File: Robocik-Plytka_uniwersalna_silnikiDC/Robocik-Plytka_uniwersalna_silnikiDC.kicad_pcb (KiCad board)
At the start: 2 copper layers, 66 parts, among them IC1 ACSL-6400-00TE, IC2 L6205D, J1 Conn_01x08, J2 Conn_01x02, J4 Conn_01x02, J6 Conn_01x02, Q1 BC847, Q2 BC847, Q3 BC847, U1 STM32F103C8Tx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

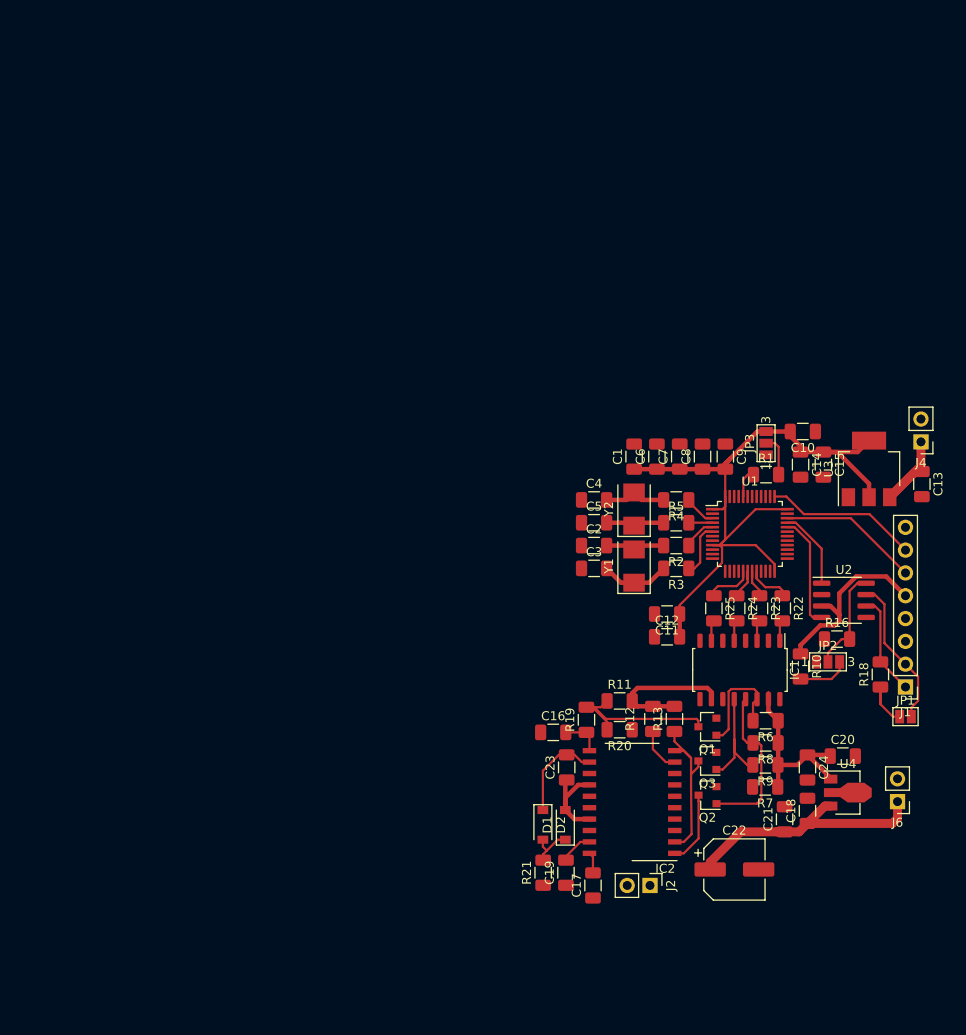
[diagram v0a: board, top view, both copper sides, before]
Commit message: Changed power supply line on schematic, added missing connections on PCB layout, added second layer connections and vias. Added layout drawing and updated schematic drawing
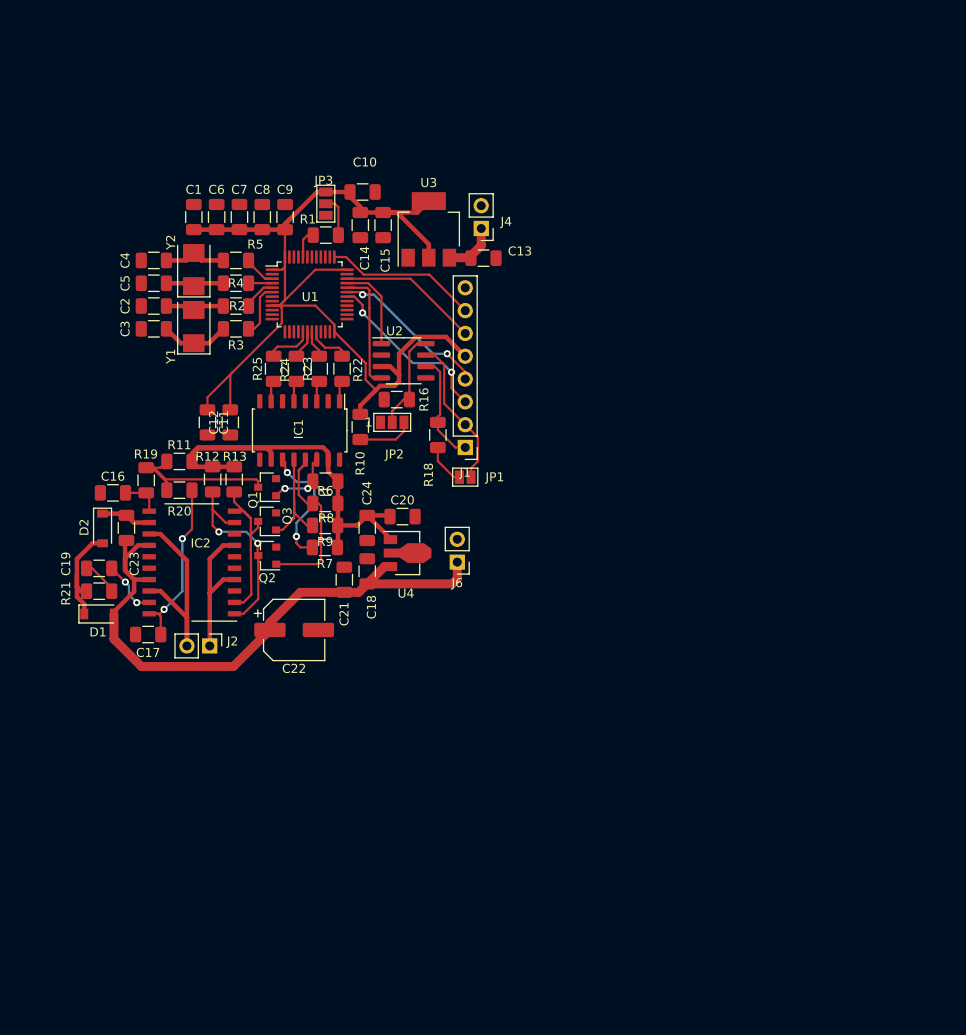
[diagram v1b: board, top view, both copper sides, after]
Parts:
- moved C19 62.1 mm to (130.9, 126.2), turned to 0 degrees
- moved D2 59.1 mm to (131.3, 121.8)
- moved R21 58.5 mm to (130.9, 128.8), turned to 180 degrees
- moved D1 57.0 mm to (130.9, 131.3), turned to 0 degrees
- moved C17 56.9 mm to (136.4, 133.6), turned to 0 degrees
- moved R18 56.0 mm to (168.7, 111.4)
- moved C21 55.8 mm to (158.2, 127.5)
- moved C24 55.8 mm to (160.8, 121.7)
- moved C7 55.8 mm to (146.6, 87.1)
- moved Q1 55.8 mm to (149.6, 117.2)
- moved Q3 55.8 mm to (149.6, 121.0)
- moved R11 55.8 mm to (139.9, 114.3)
- moved R24 55.8 mm to (152.9, 104.0)
- moved R8 55.8 mm to (156.1, 119.0)
- moved U1 55.8 mm to (154.4, 95.7)
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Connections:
- net VSSA renamed GNDA
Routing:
- net VddPWR: track 40.5 -> 68.4 mm
- net ENG2: track 0.00 -> 23.5 mm
- net USART_RX: track 0.00 -> 19.6 mm, vias 0 -> 2
- net Net-(C17-Pad2): track 2.34 -> 20.7 mm, vias 0 -> 2
- net USART_TX: track 0.00 -> 17.7 mm, vias 0 -> 2
- net ENG1: track 0.00 -> 16.5 mm
- net 5VPWR: track 37.0 -> 52.7 mm
- net 3.3VD: track 102.3 -> 117.9 mm
- net Net-(IC1-Pad11): track 0.00 -> 14.5 mm, vias 0 -> 2
- net IN1: track 13.2 -> 22.7 mm, vias 0 -> 2
- net Net-(D1-Pad1): track 5.19 -> 12.6 mm
- net VddD: track 12.4 -> 6.04 mm
- net Net-(IC1-Pad14): track 12.6 -> 8.29 mm, vias 0 -> 2
- net Net-(C23-Pad2): track 10.6 -> 6.48 mm
- net Net-(C19-Pad1): track 0.00 -> 4.07 mm
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
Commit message: Corrected GNDA and GNDD at MCU on schematic. Changed passive elements footprints from 1206 to 0805. Corrected input capacitors placement and transoptors placement. Corrected many connections on PCB. Missing: connector footprints.
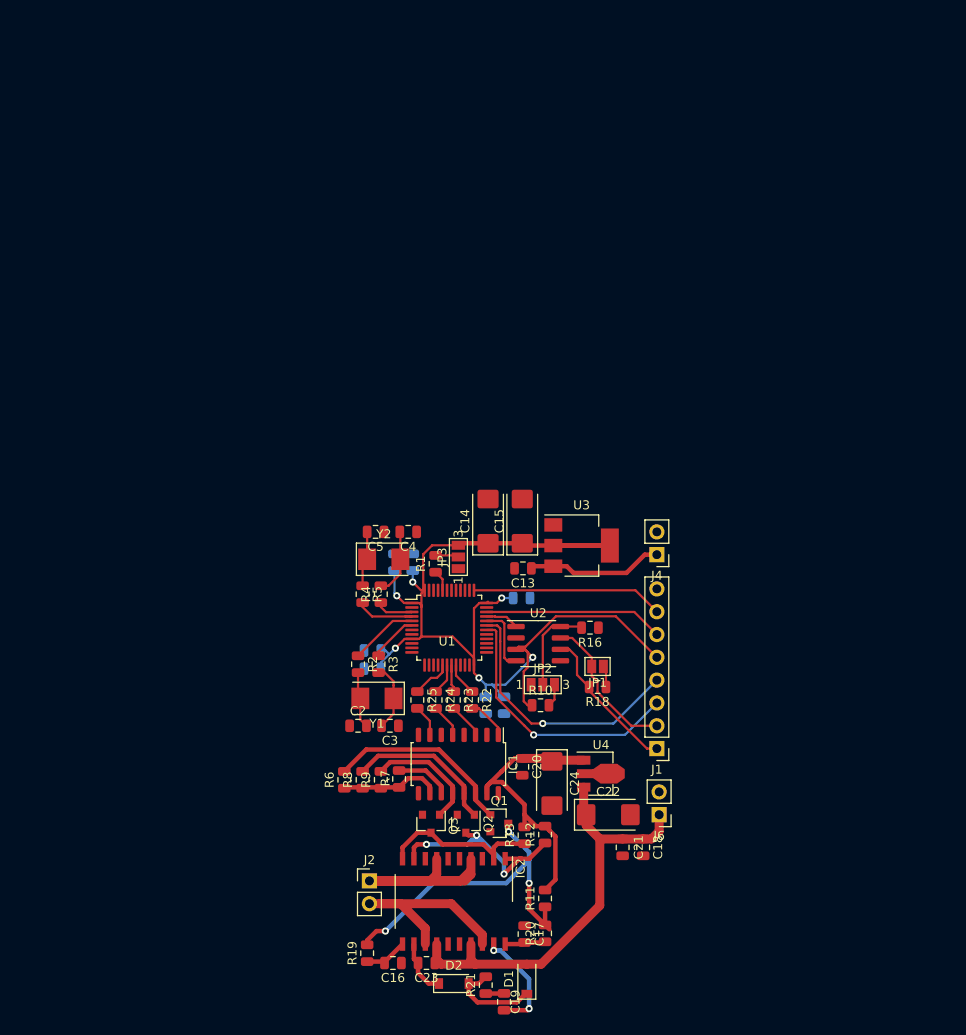
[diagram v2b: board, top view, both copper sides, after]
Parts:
- removed C8: 100nF, Capacitor_SMD:C_1206_3216Metric
- C1, C10, C11, C12, C6, C7, C9: footprint Capacitor_SMD:C_1206_3216Metric -> Capacitor_SMD:C_0805_2012Metric; moved to B.Cu
- C13, C16, C17, C18, C19, C2, C20, C21, C23, C3, C4, C5: footprint Capacitor_SMD:C_1206_3216Metric -> Capacitor_SMD:C_0805_2012Metric
- C14, C15, C24: footprint Capacitor_SMD:C_1206_3216Metric -> Capacitor_Tantalum_SMD:CP_EIA-6032-28_Kemet-C
- C22: footprint Capacitor_SMD:CP_Elec_6.3x5.8 -> Capacitor_Tantalum_SMD:CP_EIA-6032-28_Kemet-C
- R1, R10, R11, R12, R13, R16, R18, R19, R2, R20, R21, R22, R23, R24, R25, R3, R4, R5, R6, R7, R8, R9: footprint Resistor_SMD:R_1206_3216Metric -> Resistor_SMD:R_0805_2012Metric
- moved C19 66.0 mm to (176.0, 174.5), turned to 270 degrees
- moved D2 64.0 mm to (170.4, 172.5), turned to 0 degrees
- moved R20 64.0 mm to (180.6, 166.9), turned to 90 degrees
- moved R11 63.4 mm to (180.6, 163.0), turned to 90 degrees
- moved C6 63.1 mm to (176.0, 141.5), turned to 270 degrees
- moved D1 62.6 mm to (178.6, 172.0), turned to 90 degrees
- moved R21 61.5 mm to (174.0, 172.6), turned to 90 degrees
- moved C16 60.9 mm to (163.7, 170.2), turned to 180 degrees
- moved C23 58.9 mm to (167.4, 170.2), turned to 180 degrees
- moved C9 58.8 mm to (174.0, 141.5), turned to 90 degrees
- moved R19 58.1 mm to (160.8, 169.1)
- moved R12 54.2 mm to (180.6, 155.9)
- moved C17 53.6 mm to (178.3, 167.0), turned to 270 degrees
- moved C7 52.8 mm to (178.0, 129.5), turned to 0 degrees
- moved C2 52.0 mm to (159.8, 143.8)
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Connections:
- C11 pad 2: GNDA -> GNDD
- C12 pad 1: GNDA -> GNDD
- U1 pad 8: GNDA -> GNDD
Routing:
- net VddPWR: track 68.4 -> 48.4 mm
- net ENG1: track 16.5 -> 35.1 mm
- net EN: track 20.2 -> 38.7 mm, vias 0 -> 3
- net Net-(C17-Pad2): track 20.7 -> 4.55 mm, vias 2 -> 0
- net Net-(IC1-Pad14): track 8.29 -> 21.2 mm, vias 2 -> 0
- net USART_TX: track 17.7 -> 29.6 mm, vias 2 -> 1
- net USART_RX: track 19.6 -> 29.6 mm, vias 2 -> 1
- net 5VPWR: track 52.7 -> 43.0 mm
- net VddD: track 6.04 -> 15.2 mm
- net Net-(IC1-Pad11): track 14.5 -> 6.22 mm, vias 2 -> 0
- net Net-(C19-Pad2): track 6.36 -> 12.7 mm
- net CAN_TX: track 9.71 -> 3.73 mm
- net CAN_RX: track 13.5 -> 8.15 mm
- net JTMS_SWDIO: track 15.7 -> 20.0 mm
- net JTCK_SWCLK: track 17.0 -> 21.4 mm
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
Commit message: Added footprints for all connectors. Moved decoupling capacitors next to engine driver. Fixed minor mistakes on PCB layout.
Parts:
- added J3: Conn_01x04, 22-05-7045:22-05-7045, F.Cu at (169.5, 92.6)
- added J5: Conn_01x03, Connector_JST:JST_PH_S3B-PH-K_1x03_P2.00mm_Horizontal, F.Cu at (169.8, 102.1)
- J1: value Conn_01x08 -> Conn_01x03; footprint Connector_PinHeader_2.54mm:PinHeader_1x08_P2.54mm_Vertical -> 22-05-7035:SHDR3W70P0X250_1X3_990X790X510P
- J2, J6: footprint Connector_PinHeader_2.54mm:PinHeader_1x02_P2.54mm_Vertical -> Connector_Molex:Molex_Mini-Fit_Jr_5569-02A2_2x01_P4.20mm_Horizontal
- J4: footprint Connector_PinHeader_2.54mm:PinHeader_1x02_P2.54mm_Vertical -> 43650-0212:43650-0214
- moved C18 53.3 mm to (160.6, 113.8), turned to 180 degrees
- moved J4 52.1 mm to (178.1, 74.8), turned to 90 degrees
- moved R16 51.1 mm to (158.6, 89.4)
- moved R7 51.1 mm to (137.3, 106.3)
- moved U1 51.1 mm to (142.9, 89.4)
- moved U4 51.1 mm to (159.4, 105.7)
- moved C1 51.1 mm to (138.9, 82.2)
- moved C10 51.1 mm to (136.8, 82.2)
- moved C11 51.1 mm to (134.4, 92.0)
- moved C13 51.1 mm to (151.1, 82.8)
- moved C16 51.1 mm to (136.7, 126.8)
- moved C17 51.1 mm to (151.3, 123.6)
- moved C2 51.1 mm to (132.8, 100.4)
- moved C20 51.1 mm to (151.1, 104.9)
- moved C23 51.1 mm to (140.4, 126.8)
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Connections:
- J1 pad 1: CAN_L -> USART_RX
- J1 pad 2: CAN_H -> USART_TX
- J1 pad 3: USART_RX -> GNDD
- J2 pad 1: ENG1 -> ENG2
- J2 pad 2: ENG2 -> ENG1
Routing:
- net VddD: track 15.2 -> 24.6 mm
- net USART_RX: track 29.6 -> 38.7 mm, vias 1 -> 0
- net ENG1: track 35.1 -> 26.2 mm
- net USART_TX: track 29.6 -> 37.5 mm, vias 1 -> 0
- net ENG2: track 23.0 -> 30.3 mm
- net JTCK_SWCLK: track 21.4 -> 26.7 mm
- net VddPWR: track 48.4 -> 53.6 mm
- net CAN_L: track 16.7 -> 20.8 mm
- net CAN_H: track 16.7 -> 20.3 mm
- net JTMS_SWDIO: track 20.0 -> 23.3 mm
- net 3.3VD: track 114.5 -> 117.7 mm

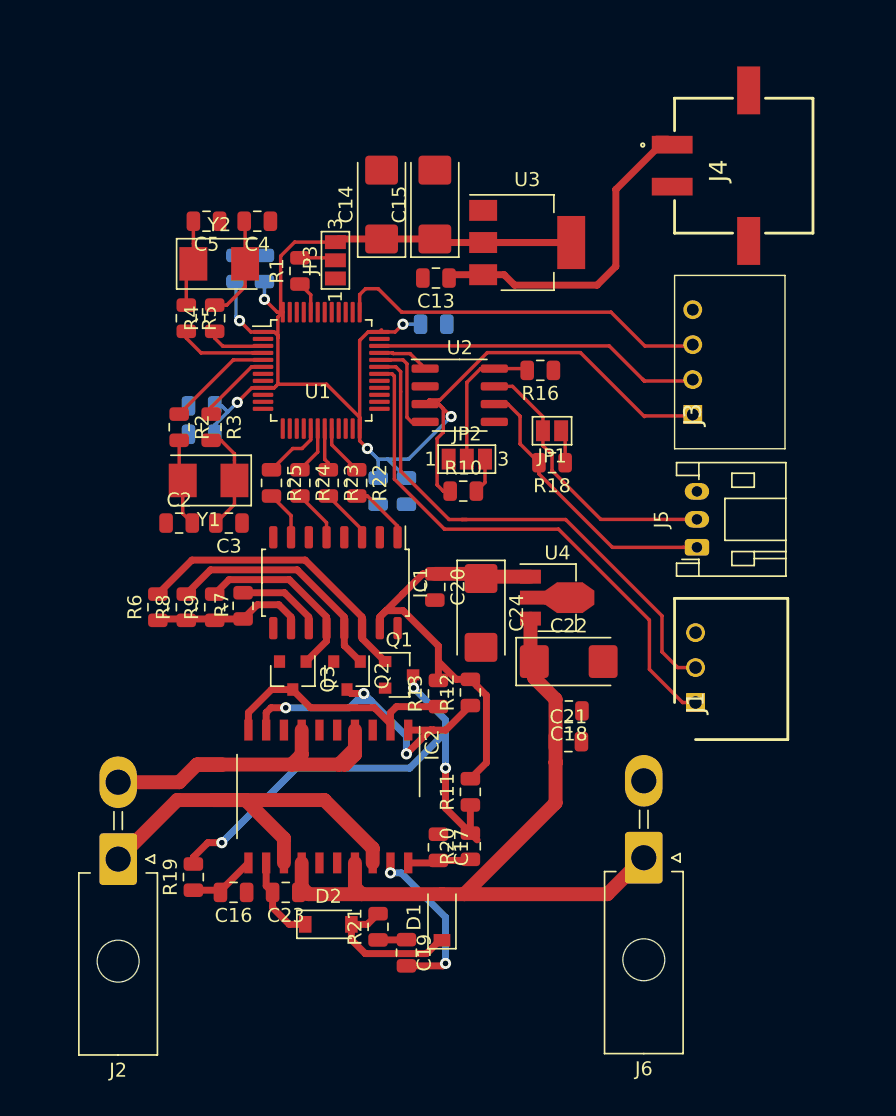
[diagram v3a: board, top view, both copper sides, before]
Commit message: Fixed power supply decoupling capacitors placement on PCB layout.
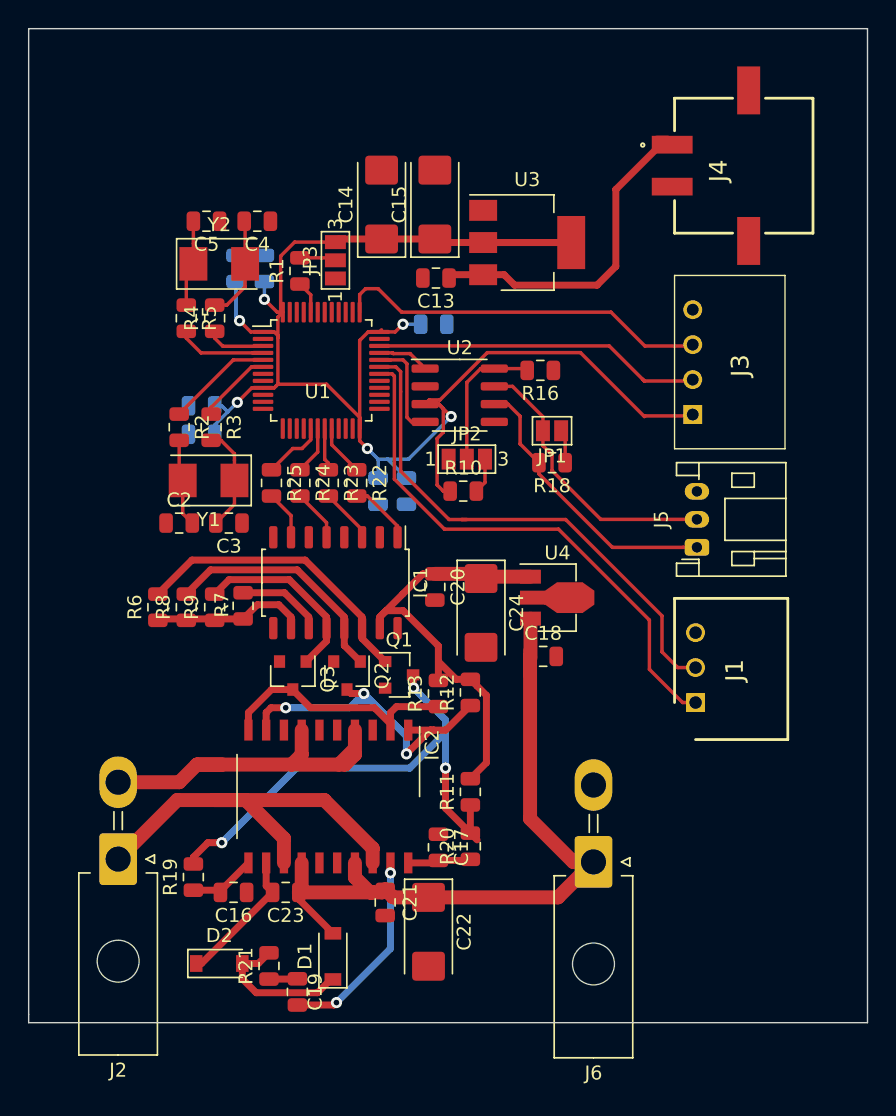
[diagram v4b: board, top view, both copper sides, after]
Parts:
- moved C22 21.8 mm to (150.6, 129.6), turned to 270 degrees
- moved C21 17.4 mm to (147.5, 127.5), turned to 270 degrees
- moved D1 8.29 mm to (143.8, 131.4)
- moved D2 8.29 mm to (135.6, 131.9)
- moved R21 8.29 mm to (139.2, 132.0)
- moved C19 8.29 mm to (141.2, 133.9)
- moved C18 4.31 mm to (158.8, 109.9), turned to 0 degrees
- moved J6 3.61 mm to (162.4, 124.6)
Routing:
- net Net-(C23-Pad2): track 6.67 -> 10.3 mm
- net Net-(C19-Pad2): track 12.7 -> 15.0 mm
- net VddPWR: track 53.6 -> 52.8 mm
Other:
- board outline added: 60 x 71.1 mm

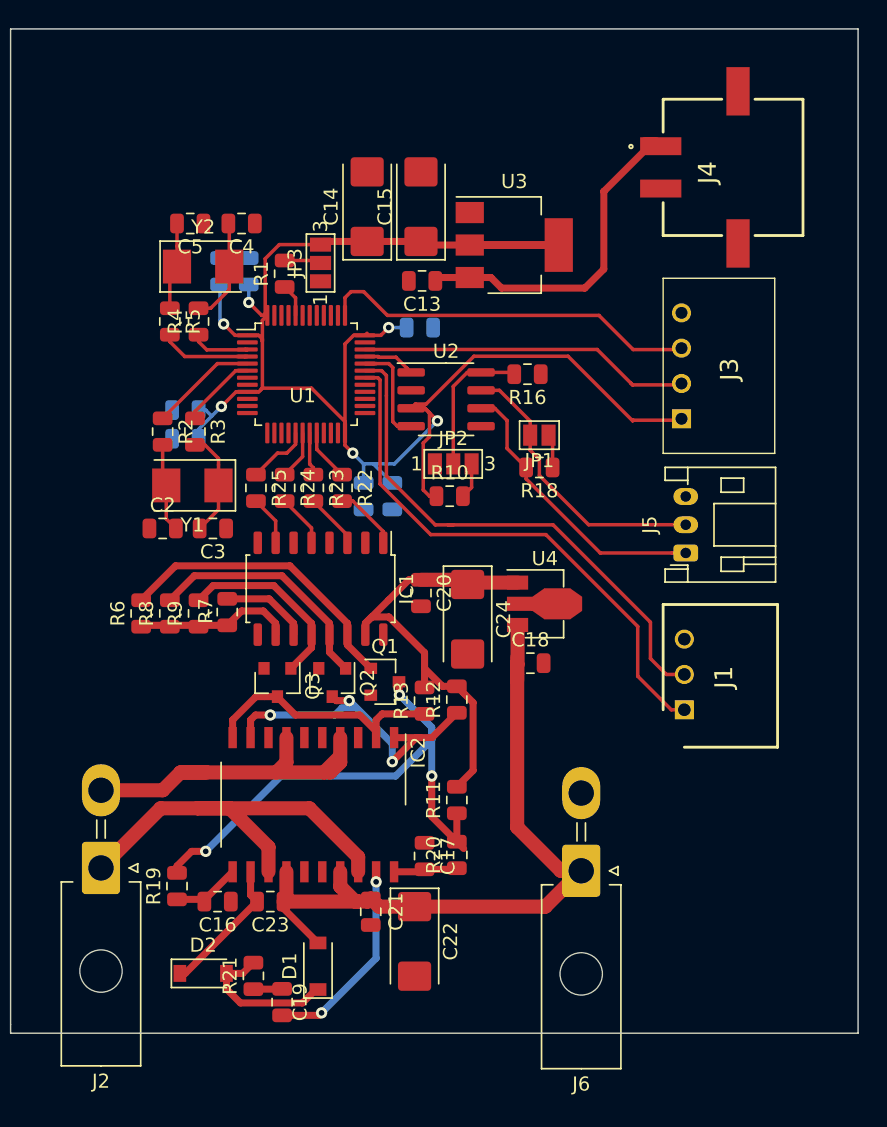
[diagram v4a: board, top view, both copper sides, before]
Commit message: Changed placements of elements, added GNDA vias, updated elements designations on PCB (not finished)
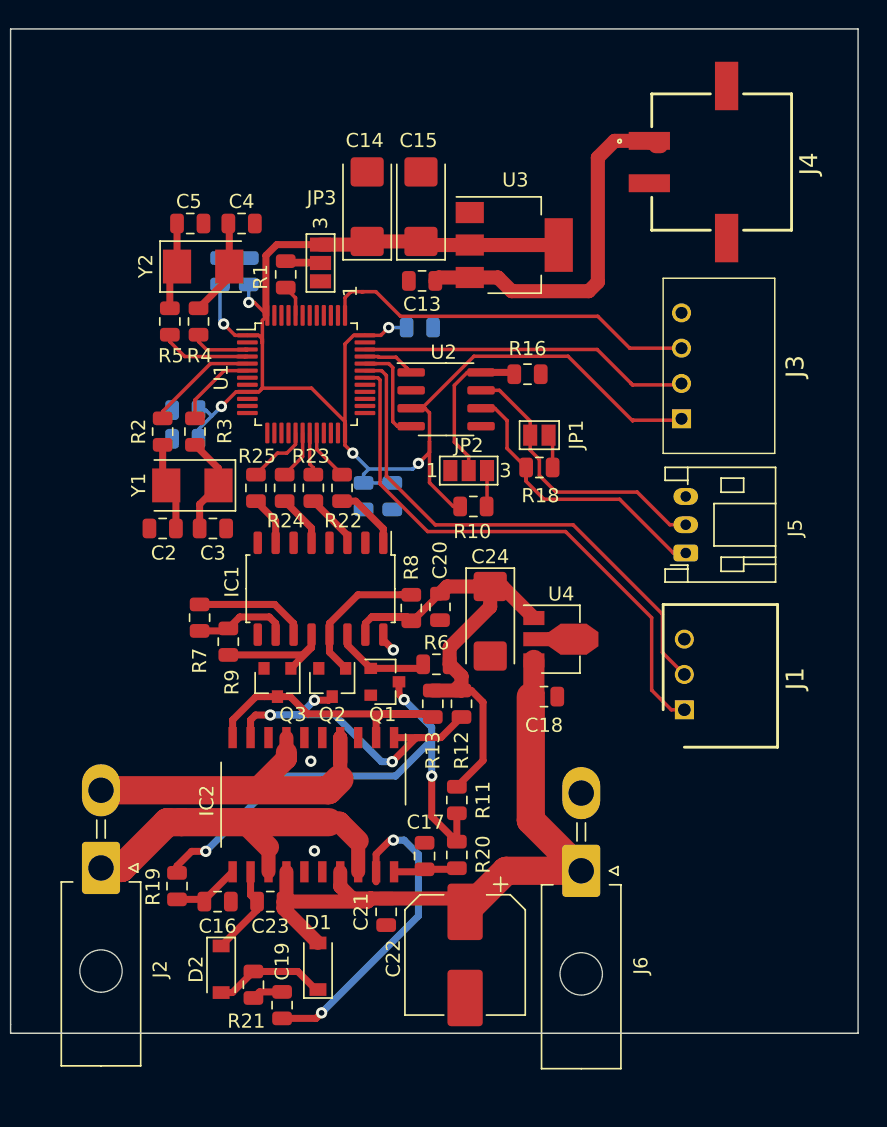
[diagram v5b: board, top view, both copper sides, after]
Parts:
- C22: footprint Capacitor_Tantalum_SMD:CP_EIA-6032-28_Kemet-C -> Capacitor_SMD:CP_Elec_8x5.4
- moved R6 21.2 mm to (152.1, 110.0), turned to 180 degrees
- moved R8 17.1 mm to (150.4, 106.0)
- moved C22 3.70 mm to (154.2, 130.6)
- moved R9 2.90 mm to (137.4, 108.4), turned to 270 degrees
- moved U4 2.76 mm to (160.5, 108.2)
- moved C18 2.56 mm to (159.8, 112.3)
- moved R7 2.00 mm to (135.4, 106.7)
- moved R10 1.83 mm to (154.8, 98.8)
- moved C20 1.67 mm to (152.4, 105.9)
- moved C24 1.61 mm to (156.0, 106.9)
- moved D2 1.31 mm to (136.9, 131.6), turned to 270 degrees
- moved JP2 1.19 mm to (154.4, 96.3)
- moved C21 1.09 mm to (148.6, 127.5)
- moved J4 0.89 mm to (177.3, 74.4)
- moved R21 0.63 mm to (139.2, 132.7)
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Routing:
- net ENG2: track 30.3 -> 47.7 mm
- net Net-(IC1-Pad14): track 21.2 -> 6.90 mm
- net ENG1: track 26.2 -> 37.5 mm
- net Net-(C19-Pad2): track 15.0 -> 23.3 mm
- net Net-(IC1-Pad13): track 17.1 -> 10.3 mm
- net 5VPWR: track 43.0 -> 48.6 mm
- net IN2: track 18.4 -> 23.7 mm
- net VddPWR: track 52.8 -> 48.9 mm
- net Net-(C23-Pad2): track 10.3 -> 6.94 mm
- net Net-(IC1-Pad12): track 13.3 -> 10.0 mm
- net VddD: track 24.6 -> 27.2 mm
- net Net-(D1-Pad1): track 10.6 -> 8.00 mm
- net Net-(JP3-Pad2): track 2.61 -> 5.13 mm
- net Net-(IC1-Pad11): track 6.22 -> 8.01 mm
- net EN: track 38.7 -> 37.2 mm
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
